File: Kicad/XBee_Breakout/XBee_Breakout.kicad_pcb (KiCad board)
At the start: 2 copper layers, 7 parts, among them J1 Conn_01x02, J2 Conn_01x04, U1 XBEE

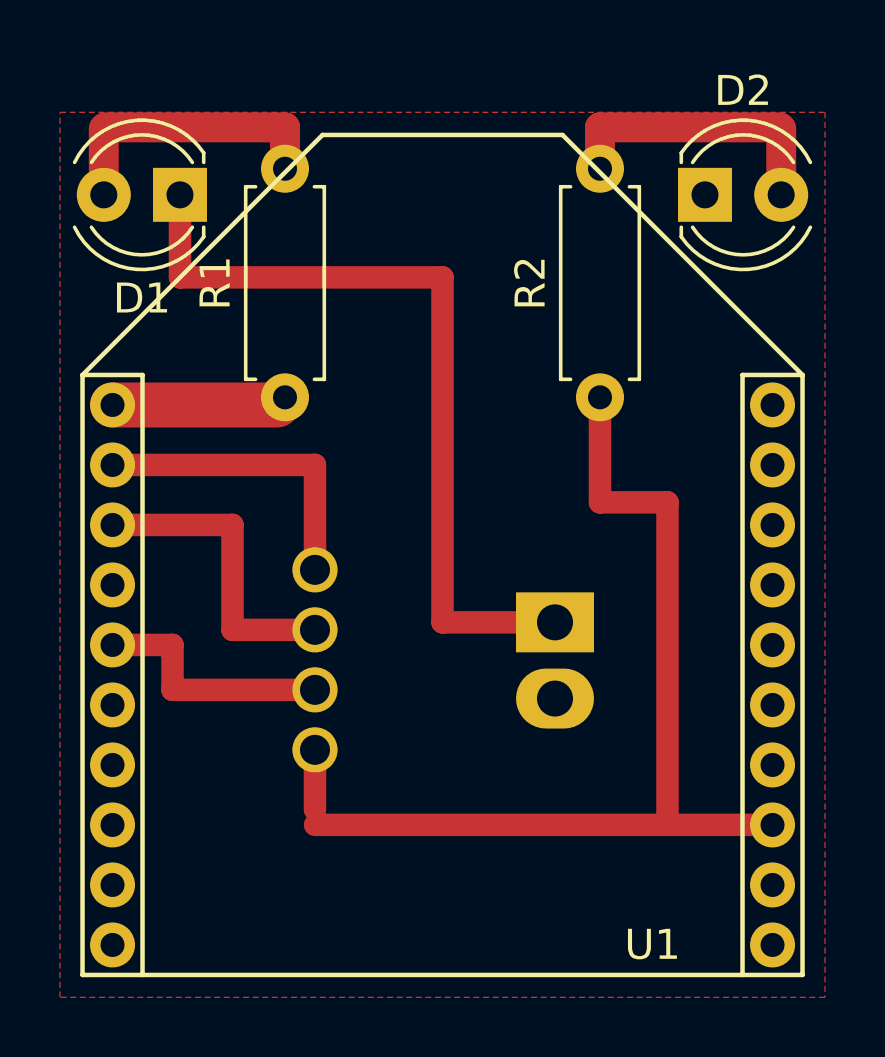
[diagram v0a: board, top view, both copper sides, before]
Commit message: Corrected 3V3 bug!
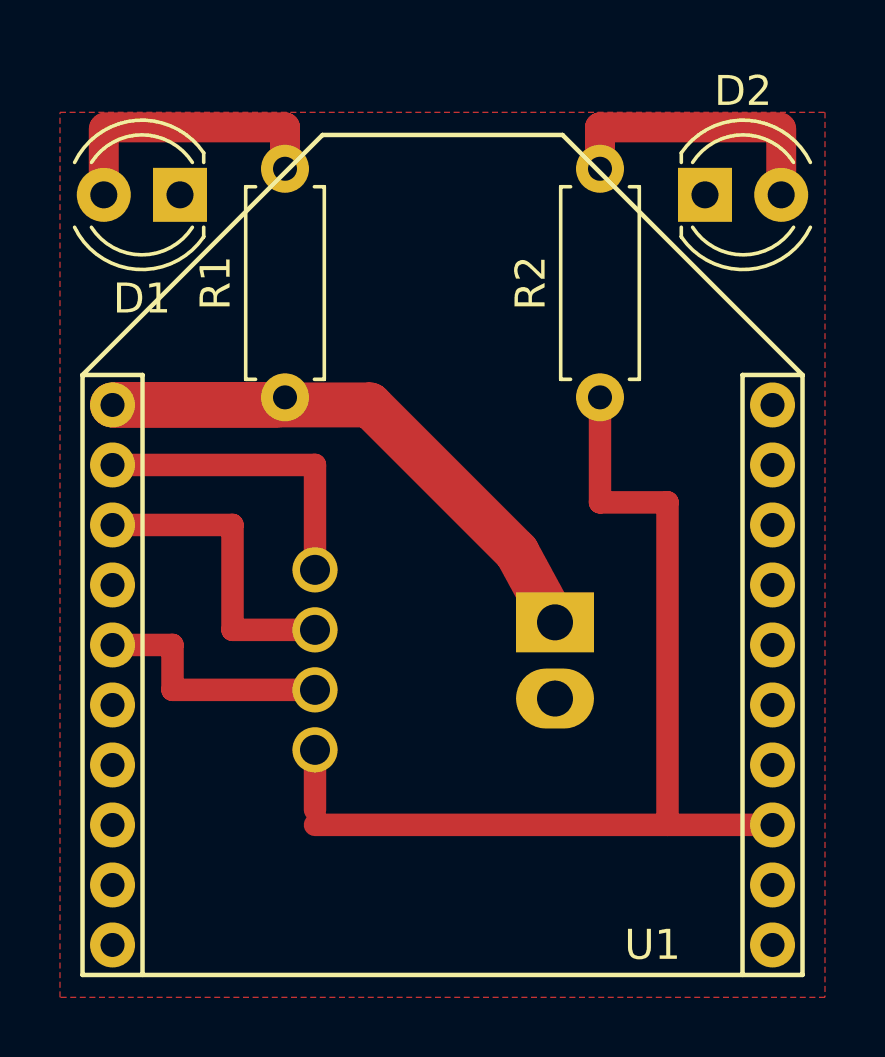
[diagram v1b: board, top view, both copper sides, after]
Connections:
- D1 pad 1: Net-(D1-Pad1) -> GND
- J1 pad 1: Net-(D1-Pad1) -> +3V3
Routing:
- net Net-(D1-Pad1): track 26.8 -> 0.00 mm
- net +3V3: track 5.85 -> 24.0 mm
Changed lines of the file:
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@@
 (kicad_pcb (version 4) (host pcbnew 4.0.7-e2-6376~58~ubuntu16.04.1)
   (general
-    (links 11)
+    (links 12)
     (no_connects 0)
-    (area 146.474999 93.515 172.525001 124.850001)
+    (area 0 0 0 0)
     (thickness 1.6)
     (drawings 5)
-    (tracks 32)
+    (tracks 31)
     (zones 0)
     (modules 7)
-    (nets 10)
+    (nets 9)
   )
   (page A4)
@@
   (net 3 "Net-(D2-Pad2)")
   (net 4 +3V3)
-  (net 5 "Net-(D1-Pad1)")
-  (net 6 /ON)
-  (net 7 /nRESET)
-  (net 8 /RX)
-  (net 9 /TX)
+  (net 5 /ON)
+  (net 6 /nRESET)
+  (net 7 /RX)
+  (net 8 /TX)
   (net_class Default "This is the default net class."
     (clearance 0.25)
@@
     (add_net /TX)
     (add_net /nRESET)
-    (add_net "Net-(D1-Pad1)")
     (add_net "Net-(D1-Pad2)")
     (add_net "Net-(D2-Pad2)")
@@
     (fp_line (start 4 -2.75) (end -1.45 -2.75) (layer F.CrtYd) (width 0.05))
     (pad 1 thru_hole rect (at 0 0 180) (size 1.8 1.8) (drill 0.9) (layers *.Cu *.Mask)
-      (net 5 "Net-(D1-Pad1)"))
+      (net 1 GND))
     (pad 2 thru_hole circle (at 2.54 0 180) (size 1.8 1.8) (drill 0.9) (layers *.Cu *.Mask)
       (net 2 "Net-(D1-Pad2)"))
@@
     )
     (pad 1 thru_hole rect (at 0 0 270) (size 2 2.6) (drill 1.2) (layers *.Cu *.Mask)
-      (net 5 "Net-(D1-Pad1)"))
+      (net 4 +3V3))
     (pad 2 thru_hole oval (at 2.54 0 270) (size 2 2.6) (drill 1.2) (layers *.Cu *.Mask)
       (net 1 GND))
@@
     (fp_line (start -5.25 -2.5) (end -5.25 2.5) (layer Dwgs.User) (width 0.127))
     (pad 1 thru_hole circle (at -3 0) (size 1.508 1.508) (drill 1) (layers *.Cu *.Mask B.SilkS)
-      (net 6 /ON) (solder_mask_margin 0.2))
+      (net 5 /ON) (solder_mask_margin 0.2))
     (pad 2 thru_hole circle (at -1 0) (size 1.508 1.508) (drill 1) (layers *.Cu *.Mask B.SilkS)
-      (net 7 /nRESET) (solder_mask_margin 0.2))
+      (net 6 /nRESET) (solder_mask_margin 0.2))
     (pad 3 thru_hole circle (at 1 0 90) (size 1.508 1.508) (drill 1) (layers *.Cu *.Mask)
-      (net 8 /RX))
+      (net 7 /RX))
     (pad 4 thru_hole circle (at 3 0 90) (size 1.508 1.508) (drill 1) (layers *.Cu *.Mask)
-      (net 9 /TX))
+      (net 8 /TX))
   )
   (module Resistors_THT:R_Axial_DIN0207_L6.3mm_D2.5mm_P7.62mm_Horizontal (layer F.Cu)
@@
     (fp_line (start 8.7 -1.6) (end -1.05 -1.6) (layer F.CrtYd) (width 0.05))
     (pad 1 thru_hole circle (at 0 0 90) (size 1.6 1.6) (drill 0.8) (layers *.Cu *.Mask)
-      (net 6 /ON))
+      (net 5 /ON))
     (pad 2 thru_hole oval (at 7.62 0 90) (size 1.6 1.6) (drill 0.8) (layers *.Cu *.Mask)
       (net 3 "Net-(D2-Pad2)"))
@@
       (net 4 +3V3))
     (pad 2 thru_hole circle (at 0 2) (size 1.5 1.5) (drill 0.8) (layers *.Cu *.Mask F.SilkS)
-      (net 9 /TX))
+      (net 8 /TX))
     (pad 3 thru_hole circle (at 0 4) (size 1.5 1.5) (drill 0.8) (layers *.Cu *.Mask F.SilkS)
-      (net 8 /RX))
+      (net 7 /RX))
     (pad 4 thru_hole circle (at 0 6) (size 1.5 1.5) (drill 0.8) (layers *.Cu *.Mask F.SilkS))
     (pad 5 thru_hole circle (at 0 8) (size 1.5 1.5) (drill 0.8) (layers *.Cu *.Mask F.SilkS)
-      (net 7 /nRESET))
+      (net 6 /nRESET))
     (pad 6 thru_hole circle (at 0 10) (size 1.5 1.5) (drill 0.8) (layers *.Cu *.Mask F.SilkS))
     (pad 7 thru_hole circle (at 0 12) (size 1.5 1.5) (drill 0.8) (layers *.Cu *.Mask F.SilkS))
@@
     (pad 12 thru_hole circle (at 22 16) (size 1.5 1.5) (drill 0.8) (layers *.Cu *.Mask F.SilkS))
     (pad 13 thru_hole circle (at 22 14) (size 1.5 1.5) (drill 0.8) (layers *.Cu *.Mask F.SilkS)
-      (net 6 /ON))
+      (net 5 /ON))
     (pad 14 thru_hole circle (at 22 12) (size 1.5 1.5) (drill 0.8) (layers *.Cu *.Mask F.SilkS))
     (pad 15 thru_hole circle (at 22 10) (size 1.5 1.5) (drill 0.8) (layers *.Cu *.Mask F.SilkS))
@@
   (segment (start 170.79 95.79) (end 170.75 95.75) (width 0.25) (layer F.Cu) (net 3))
   (segment (start 170.79 98) (end 170.79 95.79) (width 1) (layer F.Cu) (net 3))
+  (segment (start 148.5011 105.0036) (end 157.0736 105.0036) (width 1.5) (layer F.Cu) (net 4) (status 400000))
+  (segment (start 161.98 109.91) (end 163.25 112.25) (width 1.5) (layer F.Cu) (net 4) (status 800000))
+  (segment (start 157.0736 105.0036) (end 161.98 109.91) (width 1.5) (layer F.Cu) (net 4))
   (segment (start 153.9964 105.0036) (end 154.25 104.75) (width 0.25) (layer F.Cu) (net 4))
   (segment (start 148.5011 105.0036) (end 153.9964 105.0036) (width 1.5) (layer F.Cu) (net 4))
-  (segment (start 159.5 112.25) (end 163.25 112.25) (width 0.75) (layer F.Cu) (net 5))
-  (segment (start 159.5 100.75) (end 159.5 112.25) (width 0.75) (layer F.Cu) (net 5))
-  (segment (start 150.75 100.75) (end 159.5 100.75) (width 0.75) (layer F.Cu) (net 5))
-  (segment (start 150.75 98) (end 150.75 100.75) (width 0.75) (layer F.Cu) (net 5))
-  (segment (start 167 108.25) (end 167 119) (width 0.75) (layer F.Cu) (net 6))
-  (segment (start 164.75 108.25) (end 167 108.25) (width 0.75) (layer F.Cu) (net 6))
-  (segment (start 164.75 104.75) (end 164.75 108.25) (width 0.75) (layer F.Cu) (net 6))
-  (segment (start 167 119) (end 169.9975 119) (width 0.75) (layer F.Cu) (net 6))
-  (segment (start 155.25 119) (end 167 119) (width 0.75) (layer F.Cu) (net 6))
-  (segment (start 155.25 118.5) (end 155.25 119) (width 0.25) (layer F.Cu) (net 6))
-  (segment (start 155.25 116.5) (end 155.25 118.5) (width 0.75) (layer F.Cu) (net 6))
-  (segment (start 150.4964 113.0036) (end 148.5011 113.0036) (width 0.75) (layer F.Cu) (net 7))
-  (segment (start 150.5 113) (end 150.4964 113.0036) (width 0.25) (layer F.Cu) (net 7))
-  (segment (start 150.5 114.5) (end 150.5 113) (width 0.75) (layer F.Cu) (net 7))
-  (segment (start 155.25 114.5) (end 150.5 114.5) (width 0.75) (layer F.Cu) (net 7))
-  (segment (start 152.4964 109.0036) (end 148.5011 109.0036) (width 0.75) (layer F.Cu) (net 8))
-  (segment (start 152.5 109) (end 152.4964 109.0036) (width 0.25) (layer F.Cu) (net 8))
-  (segment (start 152.5 112.5) (end 152.5 109) (width 0.75) (layer F.Cu) (net 8))
-  (segment (start 155.25 112.5) (end 152.5 112.5) (width 0.75) (layer F.Cu) (net 8))
-  (segment (start 155.2464 107.0036) (end 148.5011 107.0036) (width 0.75) (layer F.Cu) (net 9))
-  (segment (start 155.25 107) (end 155.2464 107.0036) (width 0.25) (layer F.Cu) (net 9))
-  (segment (start 155.25 110.5) (end 155.25 107) (width 0.75) (layer F.Cu) (net 9))
+  (segment (start 167 108.25) (end 167 119) (width 0.75) (layer F.Cu) (net 5))
+  (segment (start 164.75 108.25) (end 167 108.25) (width 0.75) (layer F.Cu) (net 5))
+  (segment (start 164.75 104.75) (end 164.75 108.25) (width 0.75) (layer F.Cu) (net 5))
+  (segment (start 167 119) (end 169.9975 119) (width 0.75) (layer F.Cu) (net 5))
+  (segment (start 155.25 119) (end 167 119) (width 0.75) (layer F.Cu) (net 5))
+  (segment (start 155.25 118.5) (end 155.25 119) (width 0.25) (layer F.Cu) (net 5))
+  (segment (start 155.25 116.5) (end 155.25 118.5) (width 0.75) (layer F.Cu) (net 5))
+  (segment (start 150.4964 113.0036) (end 148.5011 113.0036) (width 0.75) (layer F.Cu) (net 6))
+  (segment (start 150.5 113) (end 150.4964 113.0036) (width 0.25) (layer F.Cu) (net 6))
+  (segment (start 150.5 114.5) (end 150.5 113) (width 0.75) (layer F.Cu) (net 6))
+  (segment (start 155.25 114.5) (end 150.5 114.5) (width 0.75) (layer F.Cu) (net 6))
+  (segment (start 152.4964 109.0036) (end 148.5011 109.0036) (width 0.75) (layer F.Cu) (net 7))
+  (segment (start 152.5 109) (end 152.4964 109.0036) (width 0.25) (layer F.Cu) (net 7))
+  (segment (start 152.5 112.5) (end 152.5 109) (width 0.75) (layer F.Cu) (net 7))
+  (segment (start 155.25 112.5) (end 152.5 112.5) (width 0.75) (layer F.Cu) (net 7))
+  (segment (start 155.2464 107.0036) (end 148.5011 107.0036) (width 0.75) (layer F.Cu) (net 8))
+  (segment (start 155.25 107) (end 155.2464 107.0036) (width 0.25) (layer F.Cu) (net 8))
+  (segment (start 155.25 110.5) (end 155.25 107) (width 0.75) (layer F.Cu) (net 8))
   (zone (net 1) (net_name GND) (layer F.Cu) (hatch edge 0.508)
     (connect_pads (clearance 0.508))
